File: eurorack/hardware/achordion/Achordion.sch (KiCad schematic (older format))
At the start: 120 parts, among them J1 Power, J10 Jack, J11 Jack, J2 Serial, J3 SWD, J4 Jack, J5 Jack, J6 Jack, J7 Jack, J8 Jack, J9 Jack, SW2 Button, U1 STM32F405RGT6, U10 SC39-11SURKWA, U2 LM1117-3.3, U3 LM1117-3.3, U4 LM4040B10, U5 TLV320AIC23BPW, U6 TL072, U7 MCP6002, U8 MCP6002, U9 MCP6002, Y1 8MHz

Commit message: Put down DAC OpAmp
Signed-off-by: Petr Horacek <hrck@protonmail.com>
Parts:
- C33, C34: footprint Capacitor_SMD:C_1206_3216Metric -> Capacitor_SMD:C_0603_1608Metric
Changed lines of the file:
@@
 F 0 "C33" H 15417 8296 50  0000 L CNN
 F 1 "100n" H 15425 8200 50  0000 L CNN
-F 2 "Capacitor_SMD:C_1206_3216Metric" H 15325 8250 50  0001 C CNN
+F 2 "Capacitor_SMD:C_0603_1608Metric" H 15325 8250 50  0001 C CNN
 F 3 "~" H 15325 8250 50  0001 C CNN
 	1    15325 8250
@@
 F 0 "C34" H 15417 8646 50  0000 L CNN
 F 1 "100n" H 15425 8550 50  0000 L CNN
-F 2 "Capacitor_SMD:C_1206_3216Metric" H 15325 8600 50  0001 C CNN
+F 2 "Capacitor_SMD:C_0603_1608Metric" H 15325 8600 50  0001 C CNN
 F 3 "~" H 15325 8600 50  0001 C CNN
 	1    15325 8600
@@
 	15325 8425 15325 8350
 $Comp
-L Connector:AudioJack2 J4
-U 1 1 619F540A
-P 14250 7975
-F 0 "J4" H 14070 7958 50  0000 R CNN
-F 1 "Jack" H 14070 8049 50  0000 R CNN
-F 2 "Connector_Audio:Jack_3.5mm_QingPu_WQP-PJ398SM_Vertical_CircularHoles" H 14250 7975 50  0001 C CNN
-F 3 "~" H 14250 7975 50  0001 C CNN
-	1    14250 7975
-	-1   0    0    1
-$EndComp
-$Comp
 L Device:R_Small R10
 U 1 1 61A3948C
@@
 	12875 9400 12950 9400
 $Comp
-L Device:R_Small R11
-U 1 1 61CD6251
-P 12450 9400
-F 0 "R11" H 12350 9400 50  0000 C CNN
-F 1 "47k" H 12575 9400 50  0000 C CNN
-F 2 "Resistor_SMD:R_0603_1608Metric" H 12450 9400 50  0001 C CNN
-F 3 "~" H 12450 9400 50  0001 C CNN
-	1    12450 9400
-	1    0    0    -1
-$EndComp
-$Comp
 L power:GND #PWR054
 U 1 1 61CD6257
@@
 Wire Wire Line
 	15750 8475 15750 8425
+$Comp
+L Device:R_Small R11
+U 1 1 61CD6251
+P 12450 9400
+F 0 "R11" H 12350 9400 50  0000 C CNN
+F 1 "47k" H 12575 9400 50  0000 C CNN
+F 2 "Resistor_SMD:R_0603_1608Metric" H 12450 9400 50  0001 C CNN
+F 3 "~" H 12450 9400 50  0001 C CNN
+	1    12450 9400
+	1    0    0    -1
+$EndComp
+$Comp
+L Connector:AudioJack2 J4
+U 1 1 619F540A
+P 14250 7975
+F 0 "J4" H 14070 7958 50  0000 R CNN
+F 1 "Jack" H 14070 8049 50  0000 R CNN
+F 2 "Connector_Audio:Jack_3.5mm_QingPu_WQP-PJ398SM_Vertical_CircularHoles" H 14250 7975 50  0001 C CNN
+F 3 "~" H 14250 7975 50  0001 C CNN
+	1    14250 7975
+	-1   0    0    1
+$EndComp
 $EndSCHEMATC

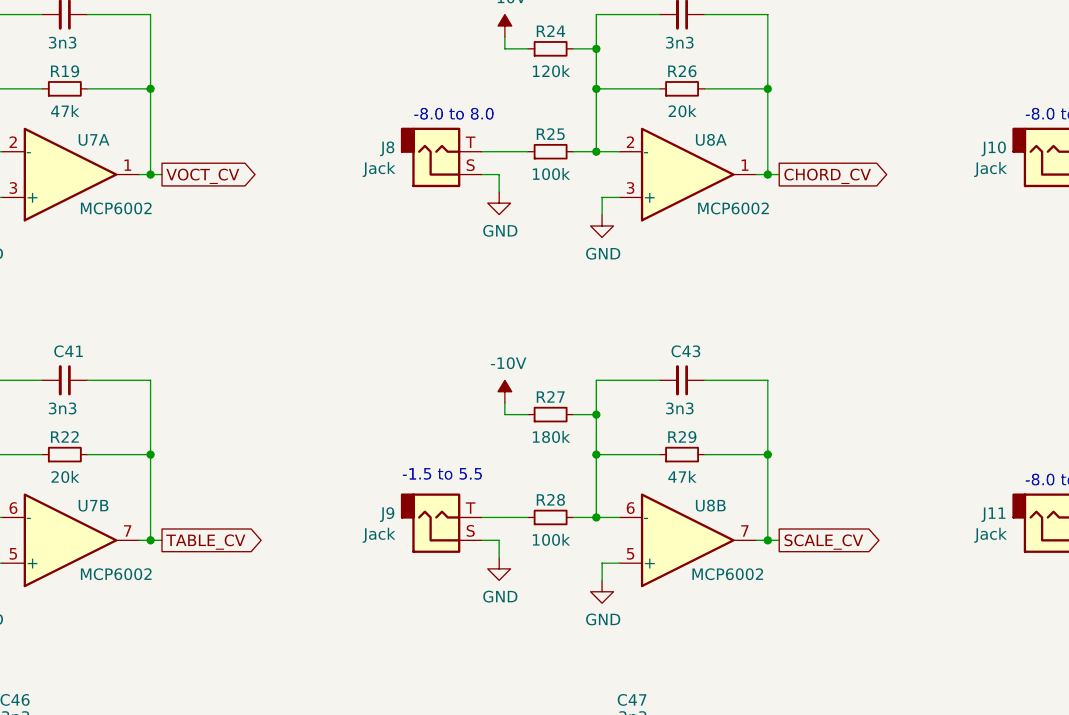
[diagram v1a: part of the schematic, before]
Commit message: Switch CVs to align horizontally on OpAmp
Signed-off-by: Petr Horacek <hrck@protonmail.com>
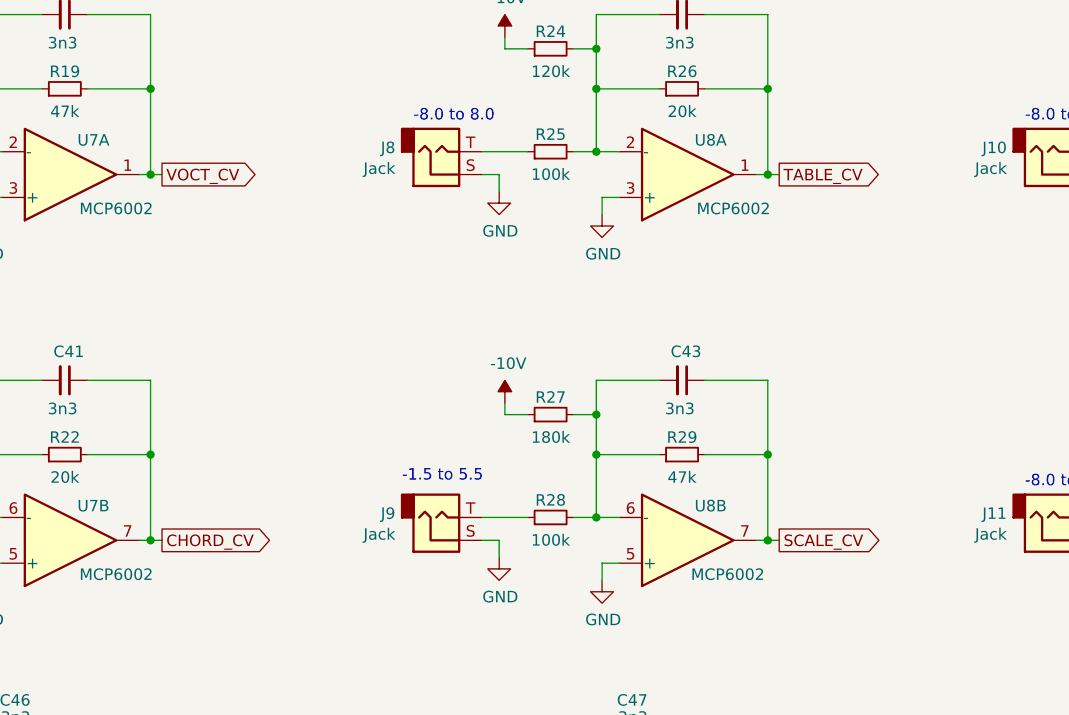
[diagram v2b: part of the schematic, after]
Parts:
- renumbered C42 to C41, C41 to C42, J8 to J7, J7 to J8, R24 to R20, R25 to R21, R26 to R22, R20 to R24, R21 to R25, R22 to R26
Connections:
- net CHORD_CV: now also U7.7; no longer U8.1
- net TABLE_CV: now also U8.1; no longer U7.7
- net at C42.2, R24.2, R25.2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: now also U8.2 (-); no longer U7.6 (-)
- net at C41.2, R20.2, R21.2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: now also U7.6 (-); no longer U8.2 (-)
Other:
- moved on the sheet: C41, C42, J7, J8, R20, R21, R22, R24, R25, R26

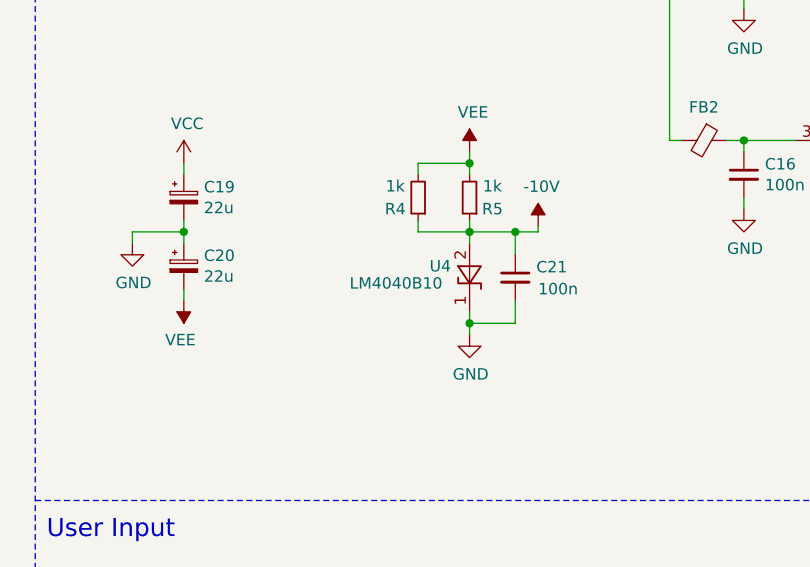
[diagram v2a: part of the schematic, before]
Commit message: Switch to LM4040C10
A10 is not available on JLCPCB.

Signed-off-by: Petr Horacek <hrck@protonmail.com>
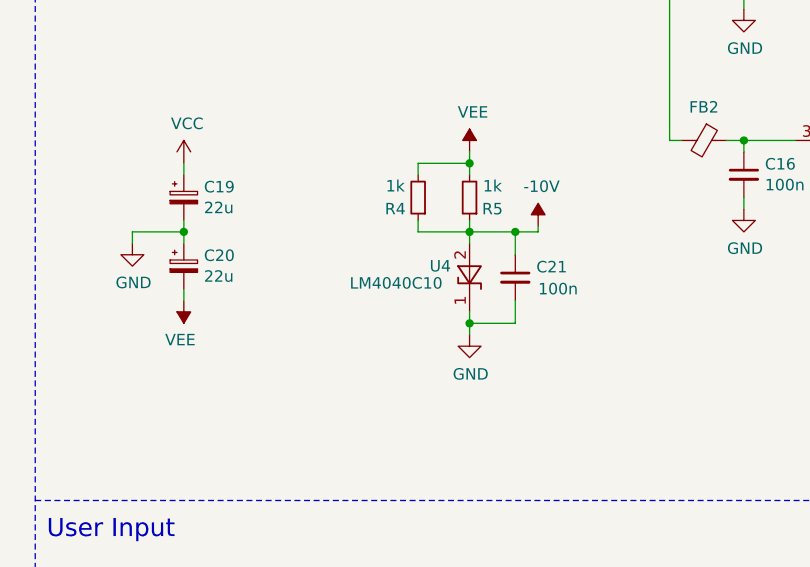
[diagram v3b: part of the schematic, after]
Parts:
- U4: value LM4040B10 -> LM4040C10
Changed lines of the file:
@@
 $EndComp
 $Comp
-L Reference_Voltage:LM4040DBZ-10 U4
-U 1 1 60B921BC
-P 12975 3200
-F 0 "U4" V 12925 3025 50  0000 L CNN
-F 1 "LM4040B10" V 13000 2675 50  0000 L CNN
-F 2 "Package_TO_SOT_SMD:SOT-23" H 12975 3000 50  0001 C CIN
-F 3 "http://www.ti.com/lit/ds/symlink/lm4040-n.pdf" H 12975 3200 50  0001 C CIN
-	1    12975 3200
-	0    1    1    0
-$EndComp
-$Comp
 L Device:R_Small R5
 U 1 1 60B7DA3E
@@
 $EndComp
 $Comp
-L Device:R_Small R18
-U 1 1 6265B422
-P 1750 7925
-F 0 "R18" V 1825 7925 50  0000 C CNN
-F 1 "100k" V 1650 7925 50  0000 C CNN
-F 2 "Resistor_SMD:R_0603_1608Metric" H 1750 7925 50  0001 C CNN
-F 3 "~" H 1750 7925 50  0001 C CNN
-	1    1750 7925
-	0    -1   -1   0
-$EndComp
-$Comp
 L power:GND #PWR069
 U 1 1 6265BDF4
@@
 	1    0    0    1
 $EndComp
+$Comp
+L Device:R_Small R18
+U 1 1 6265B422
+P 1750 7925
+F 0 "R18" V 1825 7925 50  0000 C CNN
+F 1 "100k" V 1650 7925 50  0000 C CNN
+F 2 "Resistor_SMD:R_0603_1608Metric" H 1750 7925 50  0001 C CNN
+F 3 "~" H 1750 7925 50  0001 C CNN
+	1    1750 7925
+	0    -1   -1   0
+$EndComp
+$Comp
+L Reference_Voltage:LM4040DBZ-10 U4
+U 1 1 60B921BC
+P 12975 3200
+F 0 "U4" V 12925 3025 50  0000 L CNN
+F 1 "LM4040C10" V 13000 2675 50  0000 L CNN
+F 2 "Package_TO_SOT_SMD:SOT-23" H 12975 3000 50  0001 C CIN
+F 3 "http://www.ti.com/lit/ds/symlink/lm4040-n.pdf" H 12975 3200 50  0001 C CIN
+	1    12975 3200
+	0    1    1    0
+$EndComp
 $EndSCHEMATC
